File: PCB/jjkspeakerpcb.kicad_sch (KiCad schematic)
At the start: 19 parts, among them J1 TFT 8PIN, SW1 UP, SW2 DOWN, SW3 TIME SET, SW4 CLOCK SET, SW5 SNOOZE, SW6 ALARM ON, U1 XIAO ESP32-C3

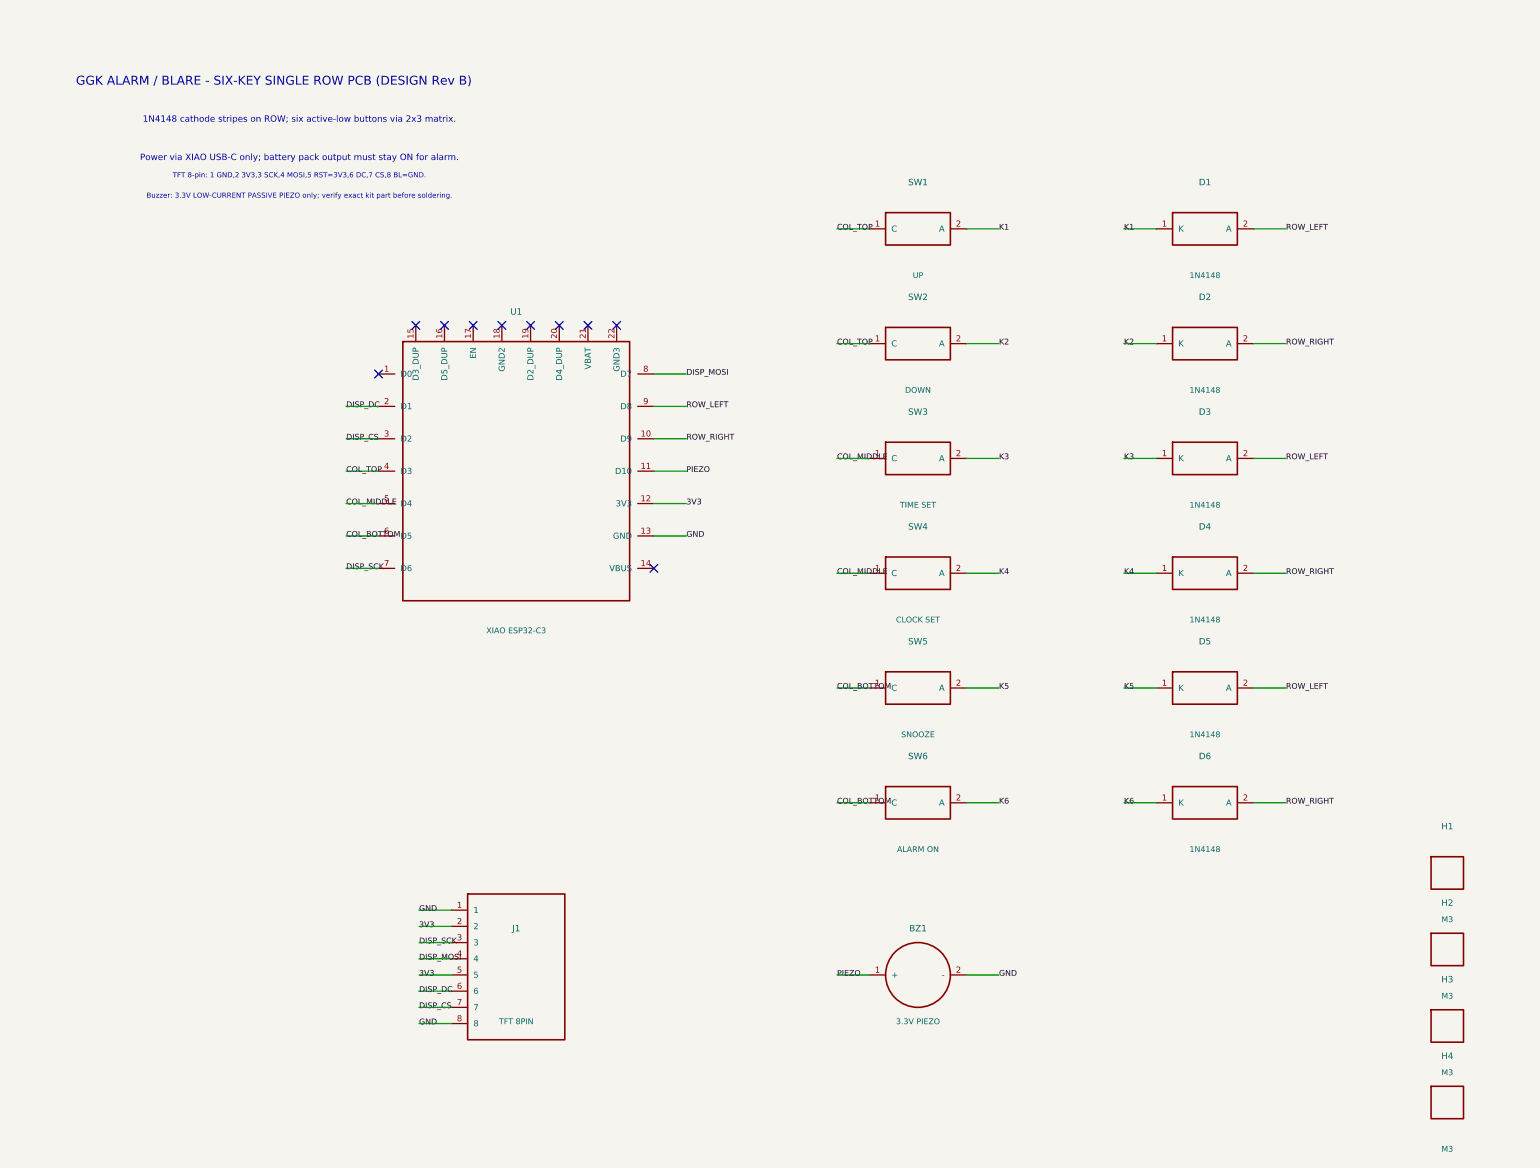
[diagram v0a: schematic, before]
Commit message: GGK Alarm Rev D: validated KiCad layout, firmware, safety gates and full build guide
* Add detailed native PCB parser diagnostics to Rev D audit gate

* Bisect native KiCad file parsing to identify invalid PCB S-expressions

* Repair malformed GND zone syntax and correct 1N4148 schematic orientation note

* Rebuild native KiCad from corrected B-side coordinates; remove overlapping holes, align schematic and nets

* Fix backside fab text mirror and regenerate local KiCad libraries for native ERC/DRC

* Diagnose remaining XIAO KiCad library mismatch using actual pcbnew geometry

* Reconstruct XIAO rear module from canonical front footprint with genuine mirrored SMD pads

* Isolate XIAO library shape mismatch: retain canonical 22 pad layout, remove redundant rear component graphics

* Correct underside pad mirroring; enforce native pad parity; regenerate board in CI

* Correct KiCad back-side pad positions and diode pin geometry using native observations

* Regenerate PCB and schematic using KiCad backside coordinates

* Fix XIAO local library mirroring to match audited board pad geometry

* Audit exact XIAO library footprint comparison using native pcbnew

* Regenerate PCB and schematic using KiCad backside coordinates

* Bundle XIAO as an exact native backside KiCad footprint for DRC comparison

* Regenerate PCB and schematic using KiCad backside coordinates

* Finish Rev D gate: filled GND zones, clean ERC DRC, real Arduino compile evidence

* Add no-extra-parts timer and stopwatch with overflow-safe tests and portrait UI

* Resolve native filled-zone thermal DRC at TFT J1 ground pad

* Regenerate PCB and schematic using KiCad backside coordinates

* Finalize Rev D evidence, verified BOM mounting, safe power guidance and release hold

* Retain mandatory DESIGN HOLD state while recording passing native KiCad checks

* Add native-KiCad verified design source synchronization before PR merge

* Restore known-good KiCad board generator and fix outdated Tinkercad SVG hole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
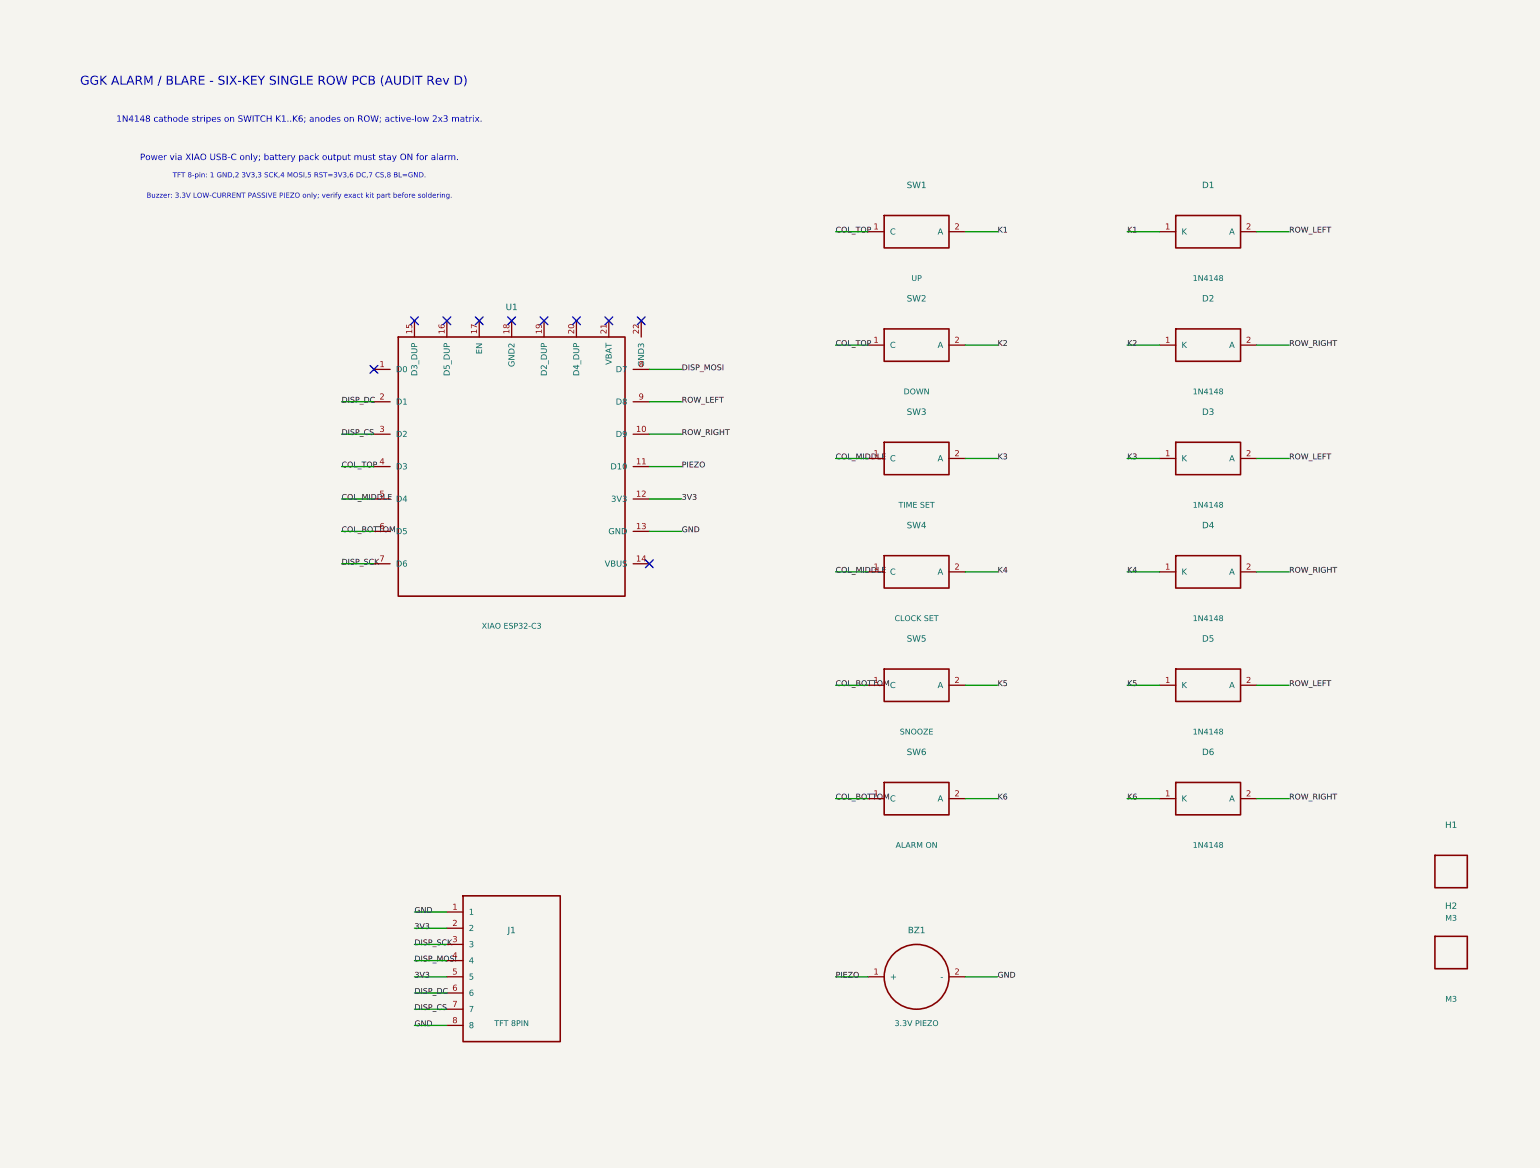
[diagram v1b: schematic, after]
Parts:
- removed H3, H4: M3, GGK:MountingHole_3.2, symbol GGK:M3_MOUNT
- H1, H2: now left out of the parts list
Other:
- note added: "1N4148 cathode stripes on SWITCH K1..K6; anodes on ROW; active-low 2x3 matrix."
- note added: "GGK ALARM / BLARE - SIX-KEY SINGLE ROW PCB (AUDIT Rev D)"
- note removed: "1N4148 cathode stripes on ROW; six active-low buttons via 2x3 matrix."
- note removed: "GGK ALARM / BLARE - SIX-KEY SINGLE ROW PCB (DESIGN Rev B)"
- moved on the sheet: D1, D2, D3, D4, D5, D6, H1, H2, J1, SW1, SW6, U1

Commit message: Stage rectangular BLARE KiCad sources, screenshots, and incomplete Gerbers (README held)
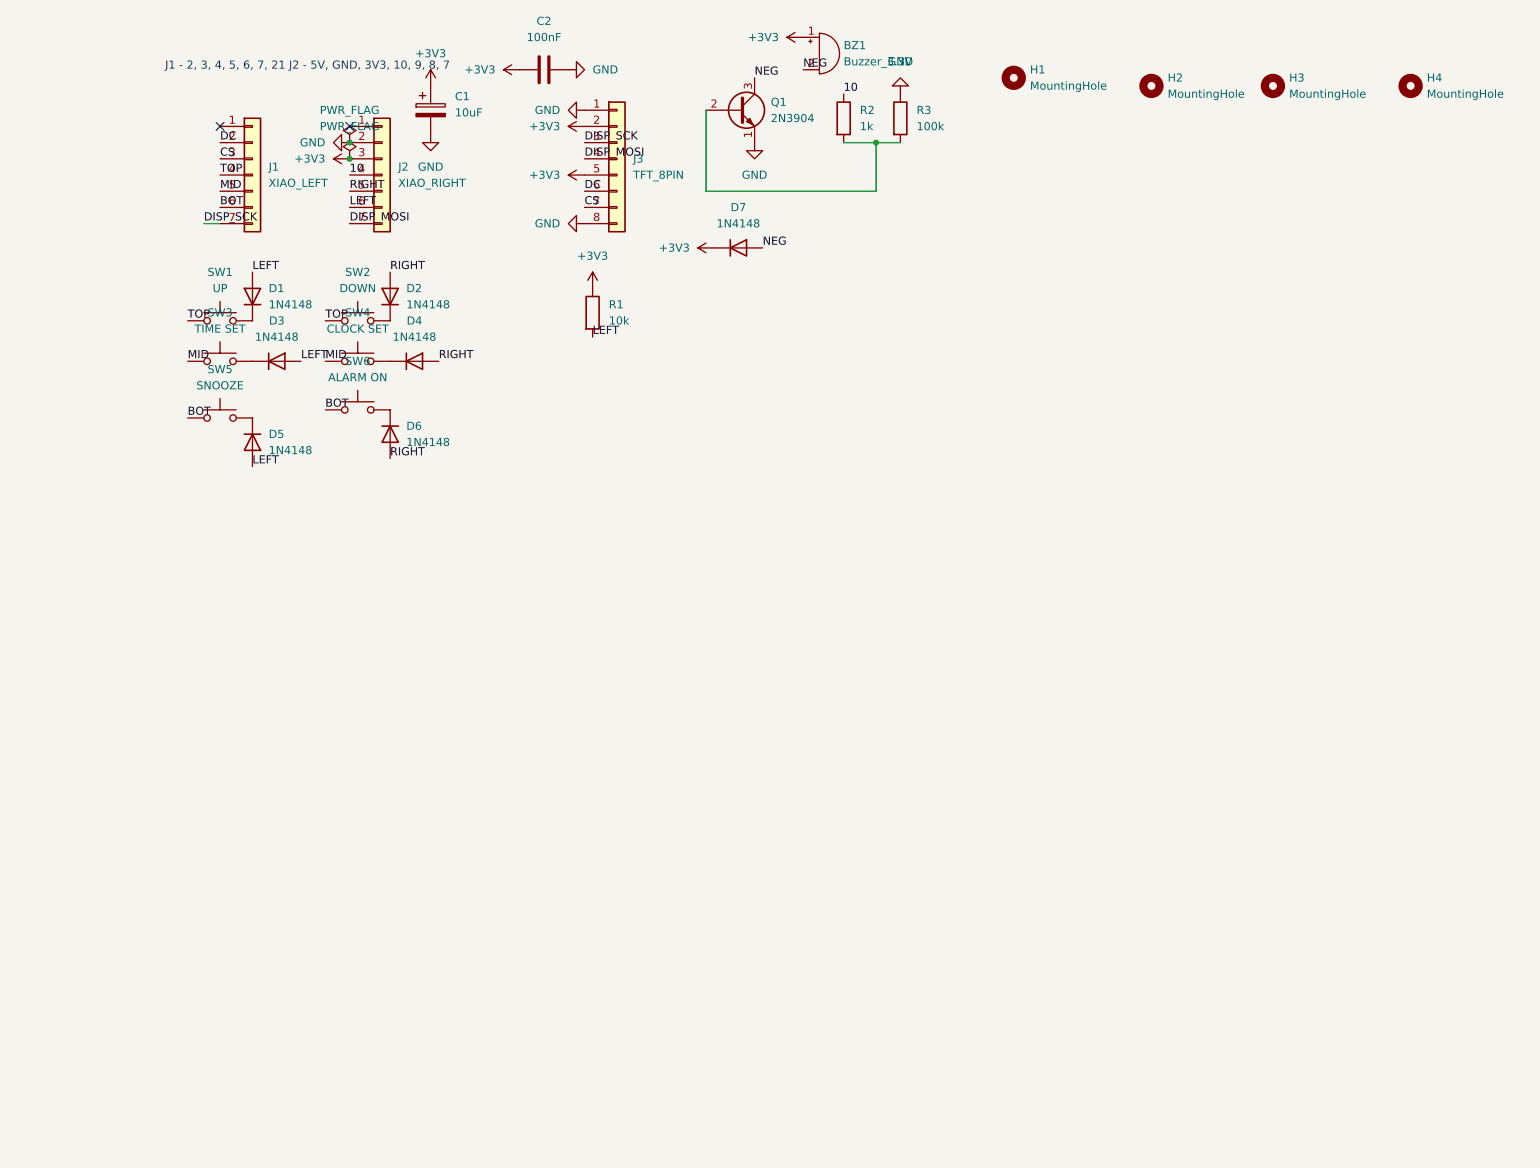
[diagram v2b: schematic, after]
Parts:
- removed BZ1: 3.3V PIEZO, GGK:Piezo_P12_P7.62, symbol GGK:PIEZO_PASSIVE
- removed D1, D2, D3, D4, D5, D6: 1N4148, GGK:D_DO35_P7.62, symbol GGK:D_DO35_P7.62
- removed H1, H2: M3, GGK:MountingHole_3.2, symbol GGK:M3_MOUNT
- removed J1: TFT 8PIN, GGK:PinHeader_1x08_2.54, symbol GGK:HEADER_TFT_1x08
- removed SW1: UP, GGK:MX_1U_PCB, symbol GGK:MX_1U_PCB
- removed SW2: DOWN, GGK:MX_1U_PCB, symbol GGK:MX_1U_PCB
- removed SW3: TIME SET, GGK:MX_1U_PCB, symbol GGK:MX_1U_PCB
- removed SW4: CLOCK SET, GGK:MX_1U_PCB, symbol GGK:MX_1U_PCB
- removed SW5: SNOOZE, GGK:MX_1U_PCB, symbol GGK:MX_1U_PCB
- removed SW6: ALARM ON, GGK:MX_1U_PCB, symbol GGK:MX_1U_PCB
- removed U1: XIAO ESP32-C3, GGK:Seeed_XIAO_ESP32C3_Castellated, symbol GGK:XIAO_ESP32_C3
- added BZ1: Buzzer_3.3V, Buzzer_Beeper:Buzzer_12x9.5RM7.6, symbol Device:Buzzer
- added C1: 10uF, Capacitor_THT:CP_Radial_D5.0mm_P2.00mm, symbol Device:C_Polarized
- added C2: 100nF, Capacitor_THT:C_Disc_D3.0mm_W1.6mm_P2.50mm, symbol Device:C
- added D1, D2, D3, D4, D5, D6, D7: 1N4148, Diode_THT:D_DO-35_SOD27_P7.62mm_Horizontal, symbol Device:D
- added H1, H2, H3, H4: MountingHole, MountingHole:MountingHole_3.2mm_M3, symbol Mechanical:MountingHole
- added J1: XIAO_LEFT, Connector_PinSocket_2.54mm:PinSocket_1x07_P2.54mm_Vertical, symbol Connector_Generic:Conn_01x07
- added J2: XIAO_RIGHT, Connector_PinSocket_2.54mm:PinSocket_1x07_P2.54mm_Vertical, symbol Connector_Generic:Conn_01x07
- added J3: TFT_8PIN, Connector_PinHeader_2.54mm:PinHeader_1x08_P2.54mm_Vertical, symbol Connector_Generic:Conn_01x08
- added Q1: 2N3904, Package_TO_SOT_THT:TO-92_Inline, symbol Transistor_BJT:2N3904
- added R1: 10k, Resistor_THT:R_Axial_DIN0207_L6.3mm_D2.5mm_P7.62mm_Horizontal, symbol Device:R
- added R2: 1k, Resistor_THT:R_Axial_DIN0207_L6.3mm_D2.5mm_P7.62mm_Horizontal, symbol Device:R
- added R3: 100k, Resistor_THT:R_Axial_DIN0207_L6.3mm_D2.5mm_P7.62mm_Horizontal, symbol Device:R
- added SW1: UP, Button_Switch_Keyboard:SW_Cherry_MX_1.00u_PCB, symbol Switch:SW_Push
- added SW2: DOWN, Button_Switch_Keyboard:SW_Cherry_MX_1.00u_PCB, symbol Switch:SW_Push
- added SW3: TIME SET, Button_Switch_Keyboard:SW_Cherry_MX_1.00u_PCB, symbol Switch:SW_Push
- added SW4: CLOCK SET, Button_Switch_Keyboard:SW_Cherry_MX_1.00u_PCB, symbol Switch:SW_Push
- added SW5: SNOOZE, Button_Switch_Keyboard:SW_Cherry_MX_1.00u_PCB, symbol Switch:SW_Push
- added SW6: ALARM ON, Button_Switch_Keyboard:SW_Cherry_MX_1.00u_PCB, symbol Switch:SW_Push
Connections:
- net DISP_MOSI: now also J2.7 (Pin_7), J3.4 (Pin_4)
- net DISP_SCK: now also J1.7 (Pin_7), J3.3 (Pin_3)
- net GND: now also C1.2, C2.2, J2.2 (Pin_2), J3.1 (Pin_1), J3.8 (Pin_8), Q1.1 (E), R3.1
- new net: Q1.2 (B), R2.2, R3.2
- new net: D1.1 (K), SW1.2
- new net: D3.1 (K), SW3.2
- new net: D5.1 (K), SW5.2
- new net: D4.1 (K), SW4.2
- new net: D6.1 (K), SW6.2
- new net: D2.1 (K), SW2.2
- new net +3V3: BZ1.1 (+), C1.1, C2.1, D7.1 (K), J2.3 (Pin_3), J3.2 (Pin_2), J3.5 (Pin_5), R1.1
- new net 10: J2.4 (Pin_4), R2.1
- new net BOT: J1.6 (Pin_6), SW5.1, SW6.1
- new net CS: J1.3 (Pin_3), J3.7 (Pin_7)
- new net DC: J1.2 (Pin_2), J3.6 (Pin_6)
- new net LEFT: D1.2 (A), D3.2 (A), D5.2 (A), J2.6 (Pin_6), R1.2
- new net MID: J1.5 (Pin_5), SW3.1, SW4.1
- new net NEG: BZ1.2 (-), D7.2 (A), Q1.3 (C)
- new net RIGHT: D2.2 (A), D4.2 (A), D6.2 (A), J2.5 (Pin_5)
- new net TOP: J1.4 (Pin_4), SW1.1, SW2.1
- no-connect marks 10 -> 2
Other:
- note added: "J1 - 2, 3, 4, 5, 6, 7, 21 J2 - 5V, GND, 3V3, 10, 9, 8, 7"
- note removed: "1N4148 cathode stripes on SWITCH K1..K6; anodes on ROW; active-low 2x3 matrix."
- note removed: "Buzzer: 3.3V LOW-CURRENT PASSIVE PIEZO only; verify exact kit part before soldering."
- note removed: "GGK ALARM / BLARE - SIX-KEY SINGLE ROW PCB (AUDIT Rev D)"
- note removed: "Power via XIAO USB-C only; battery pack output must stay ON for alarm."
- note removed: "TFT 8-pin: 1 GND,2 3V3,3 SCK,4 MOSI,5 RST=3V3,6 DC,7 CS,8 BL=GND."
